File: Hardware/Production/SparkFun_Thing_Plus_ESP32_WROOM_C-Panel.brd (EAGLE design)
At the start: 183.1 x 138.9 mm, 1532 parts, among them J10 THING_PLUS_LOGICAL, J11 QWIIC_RA, J14 MICRO-SDFRICTION, J15 THING_PLUS_LOGICAL, J16 QWIIC_RA, J19 MICRO-SDFRICTION, J2 MICRO-SDFRICTION, J20 THING_PLUS_LOGICAL, J21 QWIIC_RA, J24 MICRO-SDFRICTION, J25 THING_PLUS_LOGICAL, J26 QWIIC_RA, J29 MICRO-SDFRICTION, J3 QWIIC_RA, J30 THING_PLUS_LOGICAL, J31 QWIIC_RA, J34 MICRO-SDFRICTION, J35 THING_PLUS_LOGICAL, J36 QWIIC_RA, J39 MICRO-SDFRICTION, J40 THING_PLUS_LOGICAL, J41 QWIIC_RA, J44 MICRO-SDFRICTION, J45 THING_PLUS_LOGICAL, J46 QWIIC_RA, J49 MICRO-SDFRICTION, J5 THING_PLUS_LOGICAL, J50 THING_PLUS_LOGICAL, J51 QWIIC_RA, J54 MICRO-SDFRICTION, J55 THING_PLUS_LOGICAL, J56 QWIIC_RA, J59 MICRO-SDFRICTION, J6 QWIIC_RA, J60 THING_PLUS_LOGICAL, J61 QWIIC_RA, J64 MICRO-SDFRICTION, J65 THING_PLUS_LOGICAL, J66 QWIIC_RA, J69 MICRO-SDFRICTION, J70 THING_PLUS_LOGICAL, J9 MICRO-SDFRICTION, Q1 MBT3904DW1T1, Q10 20V/4.2A/52mΩ/1.4W, Q11 MBT3904DW1T1, Q12 20V/4.2A/52mΩ/1.4W, Q13 MBT3904DW1T1, Q14 20V/4.2A/52mΩ/1.4W, Q15 MBT3904DW1T1, Q16 20V/4.2A/52mΩ/1.4W, Q17 MBT3904DW1T1, Q18 20V/4.2A/52mΩ/1.4W, Q19 MBT3904DW1T1, Q2 MBT3904DW1T1, Q20 20V/4.2A/52mΩ/1.4W, Q21 MBT3904DW1T1, Q22 20V/4.2A/52mΩ/1.4W, Q23 MBT3904DW1T1, Q24 20V/4.2A/52mΩ/1.4W, Q25 MBT3904DW1T1, Q26 20V/4.2A/52mΩ/1.4W, Q27 MBT3904DW1T1, Q28 20V/4.2A/52mΩ/1.4W, Q3 20V/4.2A/52mΩ/1.4W, Q4 20V/4.2A/52mΩ/1.4W, Q5 MBT3904DW1T1, Q6 20V/4.2A/52mΩ/1.4W, Q7 MBT3904DW1T1, Q8 20V/4.2A/52mΩ/1.4W, Q9 MBT3904DW1T1, U1 MCP73831, U10 XC6222B331MR-G, U11 XC6222B331MR-G, U12 ESP-WROOM-3232D-NARROW, U13 MCP73831, U14 CH340C, U15 MAX17048, U16 XC6222B331MR-G, U17 XC6222B331MR-G, U18 ESP-WROOM-3232D-NARROW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

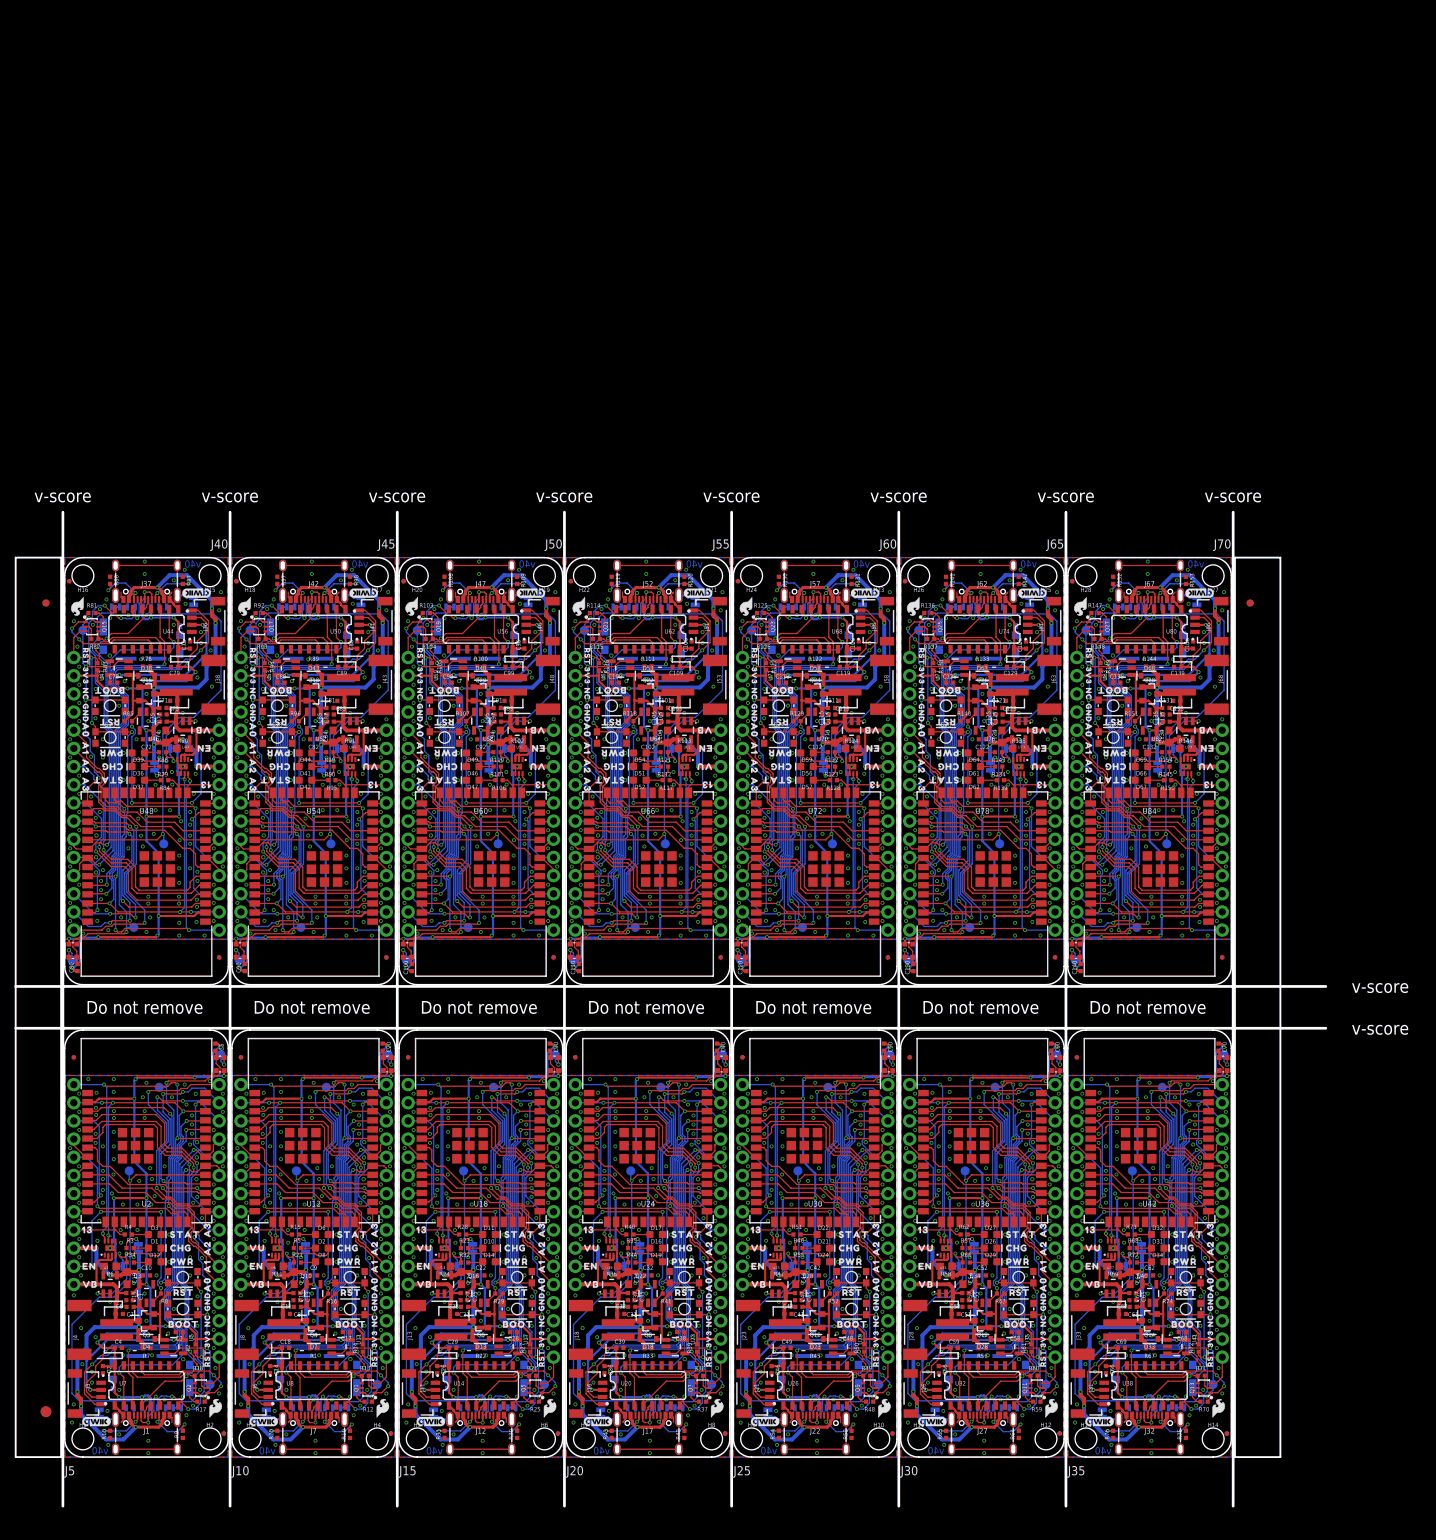
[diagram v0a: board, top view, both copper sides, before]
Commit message: Upload temp panel for Kasey.
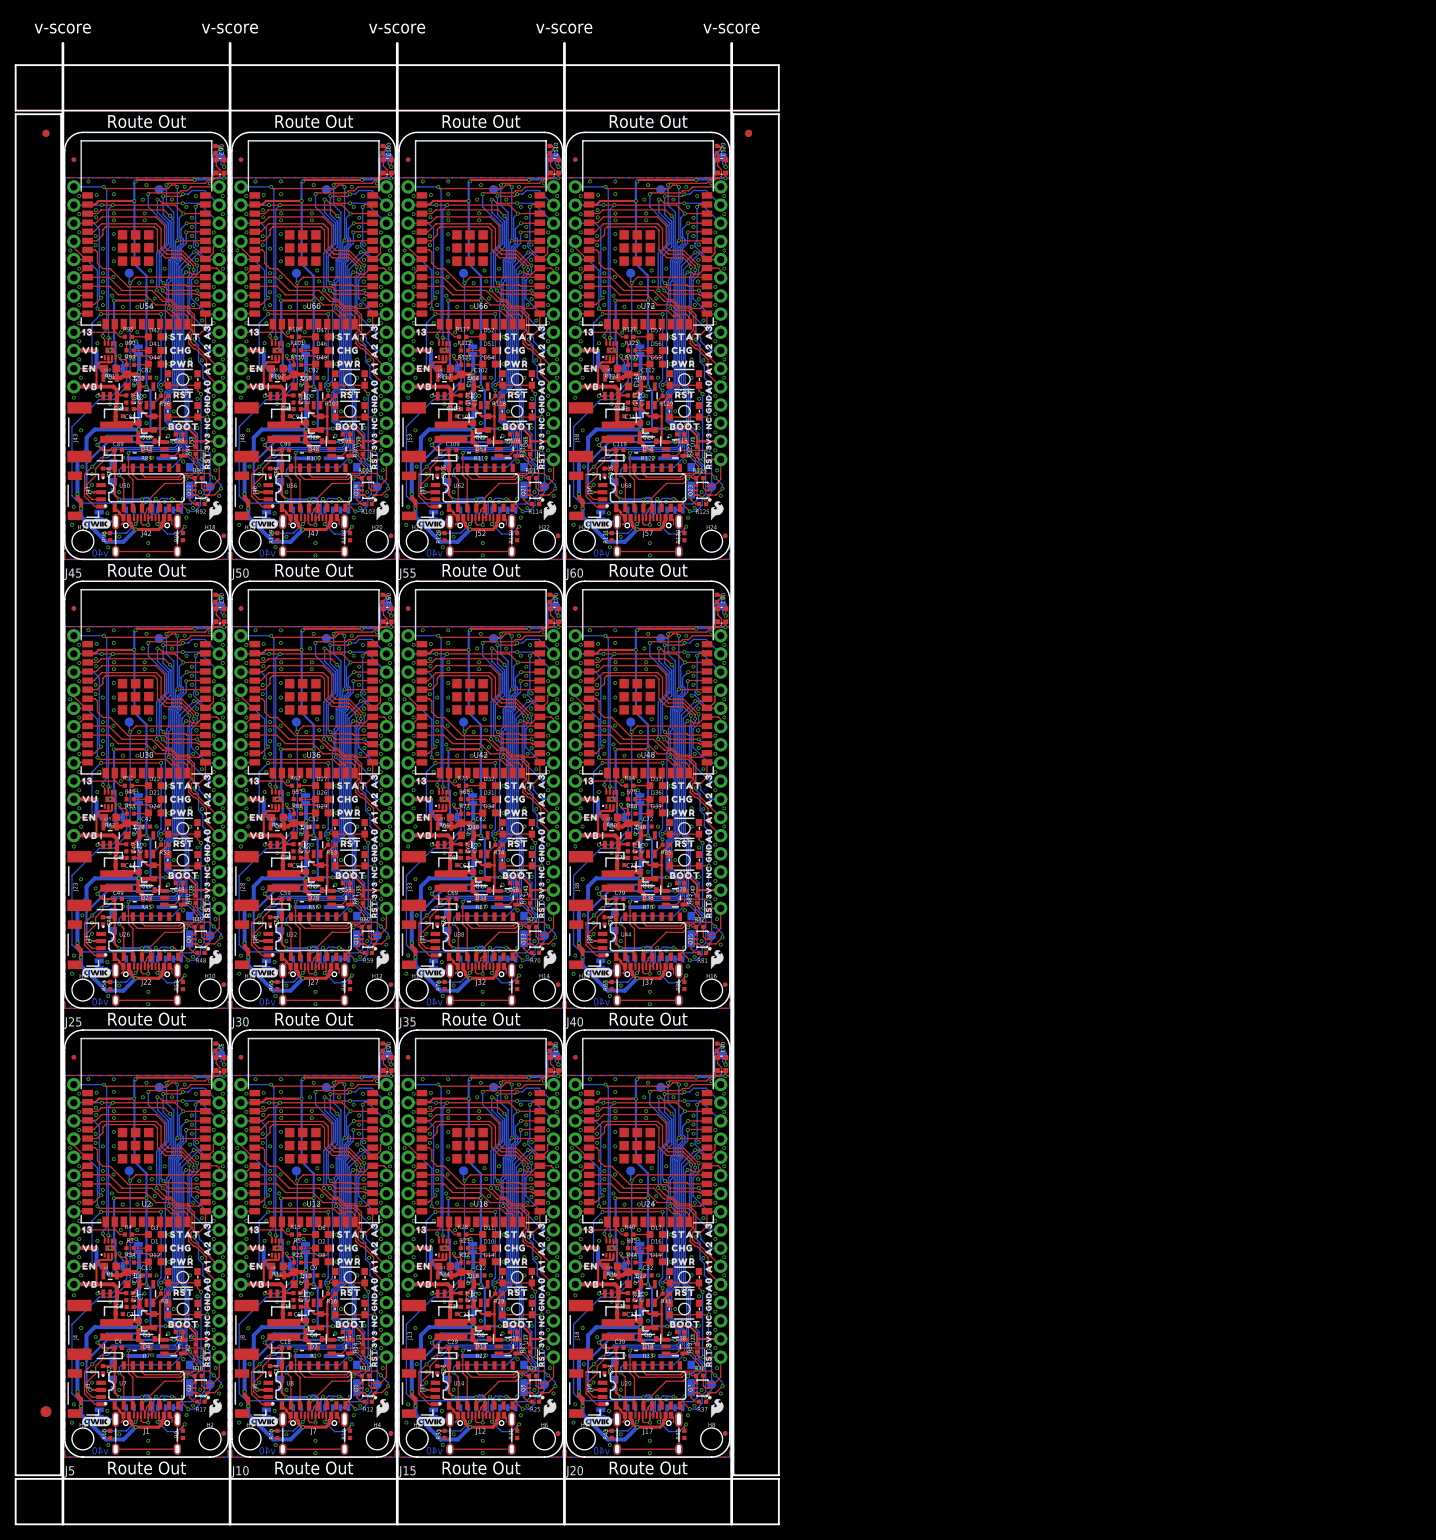
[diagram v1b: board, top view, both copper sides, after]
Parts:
- removed C121, C122, C128, C131, C132, C138: 1.0uF, SparkFun-Capacitors:0402-TIGHT
- removed C123, C133: 4.7uF, SparkFun-Capacitors:0402-TIGHT
- removed C124, C134: 4.7uF, SparkFun-Capacitors:0603
- removed C125, C130, C135, C140: 10uF, SparkFun-Capacitors:0402-TIGHT
- removed C126, C127, C129, C136, C137, C139: 0.1uF, SparkFun-Capacitors:0402-TIGHT
- removed D61, D66: Yellow, SparkFun-LED:LED-0603
- removed D62, D67: BLUE, SparkFun-LED:LED-0603
- removed D63, D68: 3A/10V/280mV, SparkFun-DiscreteSemi:SOD-323
- removed D64, D69: RED, SparkFun-LED:LED-0603
- removed D65, D70: WS2812, SparkFun-LED:WS2812-2020
- removed FD49, FD50, FD51, FD52, FD53, FD54, FD55, FD56: FIDUCIALUFIDUCIAL, SparkFun-Aesthetics:FIDUCIAL-MICRO
- removed H25, H26, H27, H28: STAND-OFFTIGHT, SparkFun-Hardware:STAND-OFF-TIGHT
- removed J61, J66: QWIIC_RA, SparkFun-Connectors:JST04_1MM_RA
- removed J62, J67: (no value), SparkFun-Connectors:USB-C-16P-2LAYER-PADS
- removed J63, J68: (no value), SparkFun-Connectors:JST-2-SMD
- removed J64, J69: MICRO-SDFRICTION, SparkFun-Connectors:MICROSD_TINY
- removed J65, J70: THING_PLUS_LOGICAL, SparkFun-Boards:THING_PLUS
- removed JP37, JP38, JP39, JP40, JP41, JP42: JUMPER-SMT_2_NC_TRACE_SILK, SparkFun-Jumpers:SMT-JUMPER_2_NC_TRACE_SILK
- removed LOGO37, LOGO40: OSHW-LOGOMINI, SparkFun-Aesthetics:OSHW-LOGO-MINI
- removed LOGO38, LOGO41: QWIIC_LOGO_4MM, SparkFun-Aesthetics:QWIIC_4MM
- removed LOGO39, LOGO42: SFE_LOGO_NAME_FLAME.1_INCH, SparkFun-Aesthetics:SFE_LOGO_NAME_FLAME_.1
- removed Q25, Q27: MBT3904DW1T1, SparkFun-DiscreteSemi:SC70-6
- removed Q26, Q28: 20V/4.2A/52mΩ/1.4W, SparkFun-DiscreteSemi:SOT23-3
- removed R133, R136, R137, R138, R140, R144, R147, R148, R149, R151: 10k, SparkFun-Resistors:0402-TIGHT
- removed R134, R139, R143, R145, R150, R154: 1k, SparkFun-Resistors:0402-TIGHT
- removed R135, R146: 2.0k, SparkFun-Resistors:0603
- removed R141, R142, R152, R153: 5.1k, SparkFun-Resistors:0402-TIGHT
- removed S25, S27: Boot, SparkFun-Switches:TACTILE_SWITCH_SMD_4.6X2.8MM
- removed S26, S28: Reset, SparkFun-Switches:TACTILE_SWITCH_SMD_4.6X2.8MM
- removed TP49, TP50, TP51, TP52, TP53, TP54, TP55, TP56: TEST-POINT3X5, SparkFun-Connectors:PAD.03X.05
- removed U$625, U$677: (no value), output:CHG1
- removed U$626, U$678: (no value), output:PWR2
- removed U$627, U$679: (no value), output:STAT0
- removed U$628, U$680: (no value), output:A03
- removed U$629, U$681: (no value), output:A12
- removed U$630, U$682: (no value), output:A21
- removed U$631, U$683: (no value), output:A30
- removed U$632, U$684: (no value), output:EN3
- removed U$633, U$685: (no value), output:130
- removed U$634, U$686: (no value), output:BOOT0
- removed U$635, U$662, U$687, U$714: (no value), output:#RST#0
- removed U$636, U$688: (no value), output:RST0
- removed U$637, U$689: (no value), output:VB1
- removed U$638, U$690: (no value), output:VU0
- removed U$639, U$691: (no value), output:3V30
- removed U$640, U$692: (no value), output:#17#TX#0
- removed U$641, U$693: (no value), output:#16#RX#0
- removed U$642, U$694: (no value), output:#18#SCK#0
- removed U$643, U$695: (no value), output:#35#A5#0
- removed U$644, U$696: (no value), output:#36#A4#0
- removed U$645, U$697: (no value), output:#25#A1#2
- removed U$646, U$698: (no value), output:#26#A0#3
- removed U$647, U$699: (no value), output:#34#A2#1
- removed U$648, U$700: (no value), output:#39#A3#0
- removed U$649, U$701: (no value), output:#12#4
- removed U$650, U$702: (no value), output:#14#9
- removed U$651, U$703: (no value), output:#15#7
- removed U$652, U$704: (no value), output:#27#5
- removed U$653, U$705: (no value), output:#32#8
- removed U$654, U$706: (no value), output:#33#6
- removed U$655, U$707: (no value), output:#EN#1
- removed U$656, U$708: (no value), output:#VBAT#0
- removed U$657, U$709: (no value), output:#VUSB#2
- removed U$658, U$710: (no value), output:#13#LED#0
- removed U$659, U$711: (no value), output:#21#SDA#1
- removed U$660, U$712: (no value), output:#22#SCL#0
- removed U$661, U$713: (no value), output:#PWR#0
- removed U$663, U$715: (no value), output:GND1
- removed U$664, U$716: (no value), output:NC0
- removed U$665, U$717: (no value), SparkFun-Aesthetics:SFE_LOGO_FLAME_STOP_.1
- removed U$666, U$718: (no value), output:#23#PICO#0
- removed U$667, U$719: (no value), output:#19#POCI#0
- removed U$668, U$720: (no value), output:#4#FREE#0
- removed U$669, U$721: (no value), output:#CHG_LED#0
- removed U$670, U$722: (no value), output:ESP32#WROOM0
- removed U$671, U$723: (no value), output:THING_PLUS_C0
- removed U$672, U$724: (no value), output:#_GND#0
- removed U$673, U$725: (no value), output:#_NC#0
- removed U$674, U$726: (no value), output:#_3V3#0
- removed U$675, U$727: (no value), SparkFun-Aesthetics:SFE_LOGO_FLAME_.1
- removed U$676, U$728: (no value), output:#SHLD#0
- removed U73, U79: MCP73831, SparkFun-IC-Power:SOT23-5
- removed U74, U80: CH340C, SparkFun-IC-Comms:SO016
- removed U75, U81: MAX17048, SparkFun-IC-Power:DFN-8
- removed U76, U77, U82, U83: XC6222B331MR-G, SparkFun-IC-Power:SOT23-5
- removed U78, U84: ESP-WROOM-3232D-NARROW, SparkFun-RF:ESP-WROOM-32D-NARROW
- moved FD33 119.8 mm to (1.27, 181.4), turned to 0 degrees
- moved FD34 119.8 mm to (1.27, 181.4), turned to 0 degrees
- moved FD37 119.8 mm to (24.6, 181.4), turned to 0 degrees
- moved FD38 119.8 mm to (24.6, 181.4), turned to 0 degrees
- moved FD41 119.8 mm to (48.0, 181.4), turned to 0 degrees
- moved FD42 119.8 mm to (48.0, 181.4), turned to 0 degrees
- moved FD45 119.8 mm to (71.4, 181.4), turned to 0 degrees
- moved FD46 119.8 mm to (71.4, 181.4), turned to 0 degrees
- moved U$462 116.4 mm to (11.4, 182.6), turned to 0 degrees
- moved U$566 116.4 mm to (58.2, 182.6), turned to 0 degrees
- moved U$514 116.4 mm to (34.8, 182.6), turned to 0 degrees
- moved U$618 116.4 mm to (81.5, 182.6), turned to 0 degrees
- moved C100 114.4 mm to (44.4, 182.8), turned to 270 degrees
- moved C110 114.4 mm to (67.8, 182.8), turned to 270 degrees
- moved C120 114.4 mm to (91.2, 182.8), turned to 270 degrees
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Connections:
- removed net !RESET!12: J65.28, Q25.3, R138.1, S26.3, S26.4, U78.3
- removed net !RESET!13: J70.28, Q27.3, R149.1, S28.3, S28.4, U84.3
- removed net 3.3V12: C122.1, C125.1, C126.1, C129.1, C130.1, D65.VCC, J64.4, J65.27, JP37.2, R138.2, U74.16, U74.4, U76.5, U78.2
- removed net 3.3V13: C132.1, C135.1, C136.1, C139.1, C140.1, D70.VCC, J69.4, J70.27, JP40.2, R149.2, U80.16, U80.4, U82.5, U84.2
- removed net CH340-DTR12: Q25.1, R136.1, U74.13
- removed net CH340-DTR13: Q27.1, R147.1, U80.13
- removed net CH340-RTS12: Q25.4, R137.1, U74.14
- removed net CH340-RTS13: Q27.4, R148.1, U80.14
- removed net CH340-RX12: U74.3, U78.35
- removed net CH340-RX13: U80.3, U84.35
- removed net CH340-TX12: U74.2, U78.34
- removed net CH340-TX13: U80.2, U84.34
- removed net CHG_LED12: D61.A, R134.2
- removed net CHG_LED13: D66.A, R145.2
- removed net D+12: J62.A6, J62.B6, U74.5
- removed net D+13: J67.A6, J67.B6, U80.5
- removed net D-12: J62.A7, J62.B7, U74.6
- removed net D-13: J67.A7, J67.B7, U80.6
- removed net DTR-10K12: Q25.5, R136.2
- removed net DTR-10K13: Q27.5, R147.2
- removed net ESP_0/QPWR12: Q25.6, S25.3, S25.4, TP49.1, U77.3, U78.25
- removed net ESP_0/QPWR13: Q27.6, S27.3, S27.4, TP53.1, U83.3, U84.25
- removed net ESP_12/GPIO13: J65.8, U78.14
- removed net ESP_12/GPIO14: J70.8, U84.14
- removed net ESP_13/GPIO0/LED12: J65.9, R139.1, U78.16
- removed net ESP_13/GPIO0/LED13: J70.9, R150.1, U84.16
- removed net ESP_14/GPIO13: J65.3, U78.13
- removed net ESP_14/GPIO14: J70.3, U84.13
- removed net ESP_15/GPIO13: J65.5, U78.23
- removed net ESP_15/GPIO14: J70.5, U84.23
- removed net ESP_16/TP_RX12: J65.15, U78.27
- removed net ESP_16/TP_RX13: J70.15, U84.27
- removed net ESP_17/TP_TX12: J65.14, U78.28
- removed net ESP_17/TP_TX13: J70.14, U84.28
- removed net ESP_18/TP_SCK12: J64.5, J65.18, U78.30
- removed net ESP_18/TP_SCK13: J69.5, J70.18, U84.30
- removed net ESP_19/TP_POCI12: J64.7, J65.16, U78.31
- removed net ESP_19/TP_POCI13: J69.7, J70.16, U84.31
- removed net ESP_2/RGB_DI12: D65.DI, TP51.1, U78.24
- removed net ESP_2/RGB_DI13: D70.DI, TP55.1, U84.24
- removed net ESP_21/TP_SDA12: J61.3, J65.1, U75.8, U78.33
- removed net ESP_21/TP_SDA13: J66.3, J70.1, U81.8, U84.33
- removed net ESP_22/TP_SCL12: J61.4, J65.2, U75.7, U78.36
- removed net ESP_22/TP_SCL13: J66.4, J70.2, U81.7, U84.36
- removed net ESP_23/TP_PICO12: J64.3, J65.17, U78.37
- removed net ESP_23/TP_PICO13: J69.3, J70.17, U84.37
- removed net ESP_25/TP_A13: J65.23, U78.10
- removed net ESP_25/TP_A14: J70.23, U84.10
- removed net ESP_26/TP_A12: J65.24, U78.11
- removed net ESP_26/TP_A13: J70.24, U84.11
- removed net ESP_27/GPIO13: J65.7, U78.12
- removed net ESP_27/GPIO14: J70.7, U84.12
- removed net ESP_32/GPIO13: J65.4, U78.8
- removed net ESP_32/GPIO14: J70.4, U84.8
- removed net ESP_33/GPIO13: J65.6, U78.9
- removed net ESP_33/GPIO14: J70.6, U84.9
- removed net ESP_34/TP_A13: J65.22, U78.6
- removed net ESP_34/TP_A14: J70.22, U84.6
- removed net ESP_35/TP_A13: J65.19, U78.7
- removed net ESP_35/TP_A14: J70.19, U84.7
- removed net ESP_36/TP_A13: J65.20, U78.4
- removed net ESP_36/TP_A14: J70.20, U84.4
- removed net ESP_39/TP_A13: J65.21, U78.5
- removed net ESP_39/TP_A14: J70.21, U84.5
- removed net ESP_4/TP_FB12: J65.13, U78.26
- removed net ESP_4/TP_FB13: J70.13, U84.26
- removed net ESP_5/SD_CS12: J64.2, TP52.1, U78.29
- removed net ESP_5/SD_CS13: J69.2, TP56.1, U84.29
- removed net GND12: C121.2, C122.2, C123.2, C124.2, C125.2, C126.2, C127.2, C128.2, C129.2, C130.2, D62.C, D64.C, D65.GND, J61.1, J62.GND, J62.GND2, J63.1, J64.6, J64.GND1, J64.GND2, J64.GND3, J64.GND4, J64.GND5, J64.GND6, J65.25, JP39.1, R133.1, R135.1, R141.1, R142.1, S25.1, S25.2, S26.1, S26.2, U73.2, U74.1, U75.1, U75.4, U75.6, U75.9, U76.2, U77.2, U78.1, U78.15, U78.38, U78.GND1, U78.GNDT1, U78.GNDT2, U78.GNDT3, U78.GNDT4, U78.GNDT5, U78.GNDT6, U78.GNDT7, U78.GNDT8
- removed net GND13: C131.2, C132.2, C133.2, C134.2, C135.2, C136.2, C137.2, C138.2, C139.2, C140.2, D67.C, D69.C, D70.GND, J66.1, J67.GND, J67.GND2, J68.1, J69.6, J69.GND1, J69.GND2, J69.GND3, J69.GND4, J69.GND5, J69.GND6, J70.25, JP42.1, R144.1, R146.1, R152.1, R153.1, S27.1, S27.2, S28.1, S28.2, U79.2, U80.1, U81.1, U81.4, U81.6, U81.9, U82.2, U83.2, U84.1, U84.15, U84.38, U84.GND1, U84.GNDT1, U84.GNDT2, U84.GNDT3, U84.GNDT4, U84.GNDT5, U84.GNDT6, U84.GNDT7, U84.GNDT8
- removed net N$145: R135.2, U73.5
- removed net N$146: D62.A, R139.2
- removed net N$147: J62.B5, R141.2
- removed net N$148: J62.A5, R142.2
- removed net N$149: D64.A, R143.2
- removed net N$150: JP37.1, R143.1
- removed net N$151: D65.DO, TP50.1
- removed net N$152: JP38.1, R134.1
- removed net N$153: D61.C, U73.1
- removed net N$156: J62.SHLD1, J62.SHLD2, J62.SHLD3, J62.SHLD4, JP39.2
- removed net N$157: R146.2, U79.5
- removed net N$158: D67.A, R150.2
- removed net N$159: J67.B5, R152.2
- removed net N$160: J67.A5, R153.2
- removed net N$161: D69.A, R154.2
- removed net N$162: JP40.1, R154.1
- removed net N$163: D70.DO, TP54.1
- removed net N$164: JP41.1, R145.1
- removed net N$165: D66.C, U79.1
- removed net N$168: J67.SHLD1, J67.SHLD2, J67.SHLD3, J67.SHLD4, JP42.2
- removed net QWIIC_PWR12: C128.1, J61.2, U77.5
- removed net QWIIC_PWR13: C138.1, J66.2, U83.5
- removed net RTS-10K12: Q25.2, R137.2
- removed net RTS-10K13: Q27.2, R148.2
- removed net TP_EN12: J65.11, R140.2, U76.3
- removed net TP_EN13: J70.11, R151.2, U82.3
- removed net VIN12: C121.1, D63.C, Q26.2, R140.1, U76.1, U77.1
- removed net VIN13: C131.1, D68.C, Q28.2, R151.1, U82.1, U83.1
- removed net V_BATT12: C123.1, C127.1, J63.2, J65.12, Q26.3, U73.3, U75.2, U75.3
- removed net V_BATT13: C133.1, C137.1, J68.2, J70.12, Q28.3, U79.3, U81.2, U81.3
- removed net V_USB12: C124.1, D63.A, J62.VBUS1, J62.VBUS2, J65.10, JP38.2, Q26.1, R133.2, U73.4
- removed net V_USB13: C134.1, D68.A, J67.VBUS1, J67.VBUS2, J70.10, JP41.2, Q28.1, R144.2, U79.4
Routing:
- net 3.3V13: track 118.3 -> 0.00 mm, vias 12 -> 0
- net 3.3V12: track 118.3 -> 0.00 mm, vias 12 -> 0
- net ESP_21/TP_SDA13: track 98.3 -> 0.00 mm, vias 5 -> 0
- net ESP_21/TP_SDA12: track 98.3 -> 0.00 mm, vias 5 -> 0
- net ESP_22/TP_SCL13: track 93.8 -> 0.00 mm, vias 5 -> 0
- net ESP_22/TP_SCL12: track 93.8 -> 0.00 mm, vias 5 -> 0
- net V_USB12: track 64.8 -> 0.00 mm, vias 7 -> 0
- net V_USB13: track 64.8 -> 0.00 mm, vias 7 -> 0
- net !RESET!12: track 60.9 -> 0.00 mm, vias 4 -> 0
- net !RESET!13: track 60.9 -> 0.00 mm, vias 4 -> 0
- net ESP_5/SD_CS13: track 56.5 -> 0.00 mm, vias 1 -> 0
- net ESP_5/SD_CS12: track 56.5 -> 0.00 mm, vias 1 -> 0
- net ESP_23/TP_PICO12: track 54.2 -> 0.00 mm, vias 5 -> 0
- net ESP_23/TP_PICO13: track 54.2 -> 0.00 mm, vias 5 -> 0
- net CH340-RX13: track 51.7 -> 0.00 mm, vias 2 -> 0
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- removed copper zone on layer 1, net GND12
- removed copper zone on layer 16, net GND12
- removed copper zone on layer 1, net GND13
- removed copper zone on layer 16, net GND13
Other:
- board size 183.1 x 138.9 mm -> 106.7 x 207 mm
- board text added: "Route Out"
- board text removed: "Do not remove"

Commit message: Updated panel
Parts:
- moved E$1 7.24 mm to (-2.62, 177.8)
- moved E$2 7.24 mm to (-2.62, 177.8)
- moved E$3 7.24 mm to (95.6, 177.8)
- moved E$4 7.24 mm to (95.6, 177.8)
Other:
- board size 106.7 x 207 mm -> 112.3 x 207 mm
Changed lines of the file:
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@@
 <rectangle x1="7.7724" y1="149.4028" x2="7.9502" y2="149.9108" layer="41"/>
 <text x="11.43" y="123.952" size="1.778" layer="20" ratio="15" align="center">Route Out</text>
-<text x="11.43" y="186.69" size="1.778" layer="20" ratio="15" align="center">Route Out</text>
 <wire x1="46.228" y1="128.016" x2="46.228" y2="182.626" width="0.2032" layer="20"/>
 <wire x1="46.228" y1="182.626" x2="43.688" y2="185.166" width="0.2032" layer="20" curve="90"/>
@@
 <rectangle x1="31.1404" y1="149.4028" x2="31.3182" y2="149.9108" layer="41"/>
 <text x="34.798" y="123.952" size="1.778" layer="20" ratio="15" align="center">Route Out</text>
-<text x="34.798" y="186.69" size="1.778" layer="20" ratio="15" align="center">Route Out</text>
 <wire x1="69.596" y1="128.016" x2="69.596" y2="182.626" width="0.2032" layer="20"/>
 <wire x1="69.596" y1="182.626" x2="67.056" y2="185.166" width="0.2032" layer="20" curve="90"/>
@@
 <rectangle x1="54.5084" y1="149.4028" x2="54.6862" y2="149.9108" layer="41"/>
 <text x="58.166" y="123.952" size="1.778" layer="20" ratio="15" align="center">Route Out</text>
-<text x="58.166" y="186.69" size="1.778" layer="20" ratio="15" align="center">Route Out</text>
 <wire x1="92.964" y1="128.016" x2="92.964" y2="182.626" width="0.2032" layer="20"/>
 <wire x1="92.964" y1="182.626" x2="90.424" y2="185.166" width="0.2032" layer="20" curve="90"/>
@@
 <rectangle x1="77.8764" y1="149.4028" x2="78.0542" y2="149.9108" layer="41"/>
 <text x="81.534" y="123.952" size="1.778" layer="20" ratio="15" align="center">Route Out</text>
-<text x="81.534" y="186.69" size="1.778" layer="20" ratio="15" align="center">Route Out</text>
 <wire x1="-0.254" y1="-9.398" x2="-0.254" y2="197.612" width="0.381" layer="46"/>
 <text x="-0.254" y="199.898" size="1.778" layer="46" ratio="15" align="center">v-score</text>
@@
 <wire x1="99.822" y1="-9.398" x2="-6.858" y2="-9.398" width="0.254" layer="20"/>
 <wire x1="-6.858" y1="-9.398" x2="-6.858" y2="-3.048" width="0.254" layer="20"/>
-<wire x1="93.472" y1="187.706" x2="99.822" y2="187.706" width="0.254" layer="20"/>
-<wire x1="99.822" y1="187.706" x2="99.822" y2="-2.54" width="0.254" layer="20"/>
+<wire x1="93.472" y1="185.166" x2="99.822" y2="185.166" width="0.254" layer="20"/>
+<wire x1="99.822" y1="185.166" x2="99.822" y2="-2.54" width="0.254" layer="20"/>
 <wire x1="99.822" y1="-2.54" x2="93.472" y2="-2.54" width="0.254" layer="20"/>
-<wire x1="93.472" y1="-2.54" x2="93.472" y2="187.706" width="0.254" layer="20"/>
-<wire x1="-6.858" y1="194.564" x2="99.822" y2="194.564" width="0.254" layer="20"/>
-<wire x1="99.822" y1="194.564" x2="99.822" y2="188.214" width="0.254" layer="20"/>
-<wire x1="99.822" y1="188.214" x2="-6.858" y2="188.214" width="0.254" layer="20"/>
-<wire x1="-6.858" y1="188.214" x2="-6.858" y2="194.564" width="0.254" layer="20"/>
-<wire x1="-6.858" y1="187.706" x2="-0.508" y2="187.706" width="0.254" layer="20"/>
-<wire x1="-0.508" y1="187.706" x2="-0.508" y2="-2.54" width="0.254" layer="20"/>
+<wire x1="93.472" y1="-2.54" x2="93.472" y2="185.166" width="0.254" layer="20"/>
+<wire x1="-6.858" y1="192.024" x2="99.822" y2="192.024" width="0.254" layer="20"/>
+<wire x1="99.822" y1="192.024" x2="99.822" y2="185.674" width="0.254" layer="20"/>
+<wire x1="99.822" y1="185.674" x2="-6.858" y2="185.674" width="0.254" layer="20"/>
+<wire x1="-6.858" y1="185.674" x2="-6.858" y2="192.024" width="0.254" layer="20"/>
+<wire x1="-6.858" y1="185.166" x2="-0.508" y2="185.166" width="0.254" layer="20"/>
+<wire x1="-0.508" y1="185.166" x2="-0.508" y2="-2.54" width="0.254" layer="20"/>
 <wire x1="-0.508" y1="-2.54" x2="-6.858" y2="-2.54" width="0.254" layer="20"/>
-<wire x1="-6.858" y1="-2.54" x2="-6.858" y2="187.706" width="0.254" layer="20"/>
+<wire x1="-6.858" y1="-2.54" x2="-6.858" y2="185.166" width="0.254" layer="20"/>
+<wire x1="-6.858" y1="185.42" x2="105.41" y2="185.42" width="0.381" layer="46"/>
+<text x="110.49" y="185.674" size="1.778" layer="46" ratio="15" align="center">v-score</text>
 </plain>
 <attributes>
@@
 <element name="U$623" library="SparkFun-Aesthetics" package="SFE_LOGO_FLAME_.1" value="" x="91.186" y="132.334" smashed="yes"/>
 <element name="U$624" library="output" package="#SHLD#0" value="" x="74.93" y="132.4102" smashed="yes" rot="MR90"/>
-<element name="E$1" library="SparkFun-Aesthetics" package="FIDUCIAL-1X2" value="" x="-2.62381875" y="185.039" smashed="yes"/>
-<element name="E$2" library="SparkFun-Aesthetics" package="FIDUCIAL-1X2" value="" x="-2.62381875" y="185.039" smashed="yes" rot="MR0"/>
-<element name="E$3" library="SparkFun-Aesthetics" package="FIDUCIAL-1X2" value="" x="95.58781875" y="185.039" smashed="yes"/>
-<element name="E$4" library="SparkFun-Aesthetics" package="FIDUCIAL-1X2" value="" x="95.58781875" y="185.039" smashed="yes" rot="MR0"/>
+<element name="E$1" library="SparkFun-Aesthetics" package="FIDUCIAL-1X2" value="" x="-2.62381875" y="177.8" smashed="yes"/>
+<element name="E$2" library="SparkFun-Aesthetics" package="FIDUCIAL-1X2" value="" x="-2.62381875" y="177.8" smashed="yes" rot="MR0"/>
+<element name="E$3" library="SparkFun-Aesthetics" package="FIDUCIAL-1X2" value="" x="95.58781875" y="177.8" smashed="yes"/>
+<element name="E$4" library="SparkFun-Aesthetics" package="FIDUCIAL-1X2" value="" x="95.58781875" y="177.8" smashed="yes" rot="MR0"/>
 <element name="E$5" library="SparkFun-Retired" package="FIDUCIAL-1.5X3" value="" x="-2.62381875" y="6.35" smashed="yes"/>
 <element name="E$6" library="SparkFun-Retired" package="FIDUCIAL-1.5X3" value="" x="-2.62381875" y="6.35" smashed="yes" rot="MR0"/>
